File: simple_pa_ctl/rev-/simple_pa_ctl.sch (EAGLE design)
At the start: 93 parts, among them IC1 LD117ADT50TR, IC2 MCP9700, IC3 ATMEGA32U4-AU, J1 USB_B_PTH, K3 G5V1, SW1 SPST_TACT-KMR2, Y1 8MHz

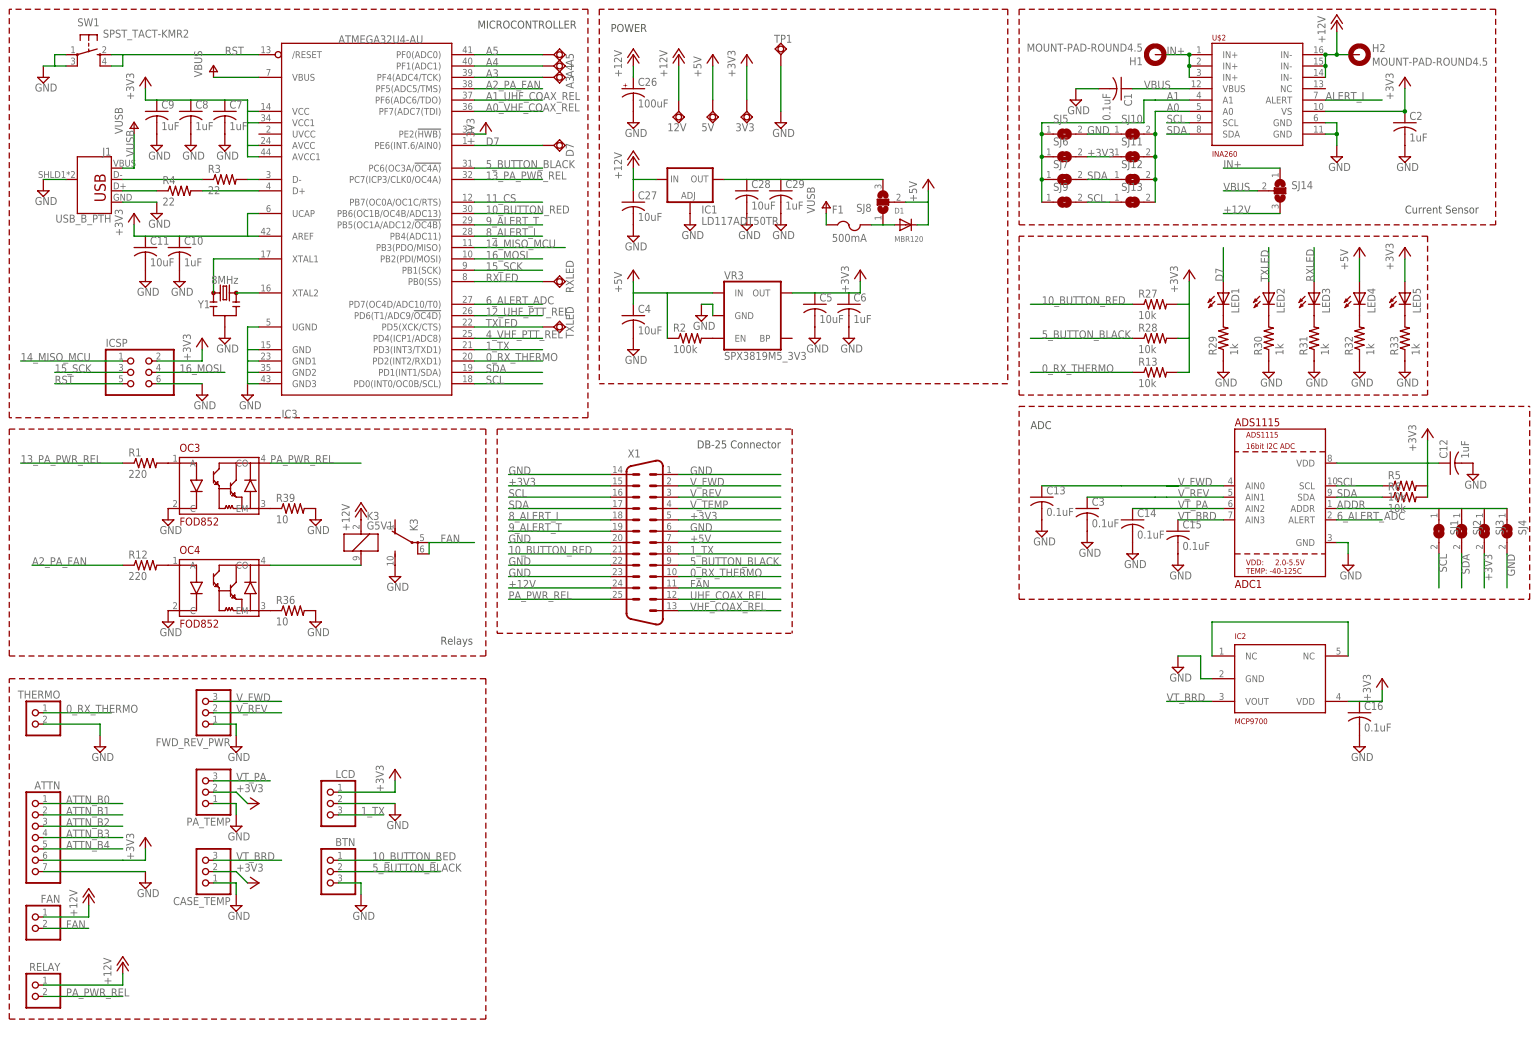
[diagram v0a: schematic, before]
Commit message: very simple, featherwing footprint
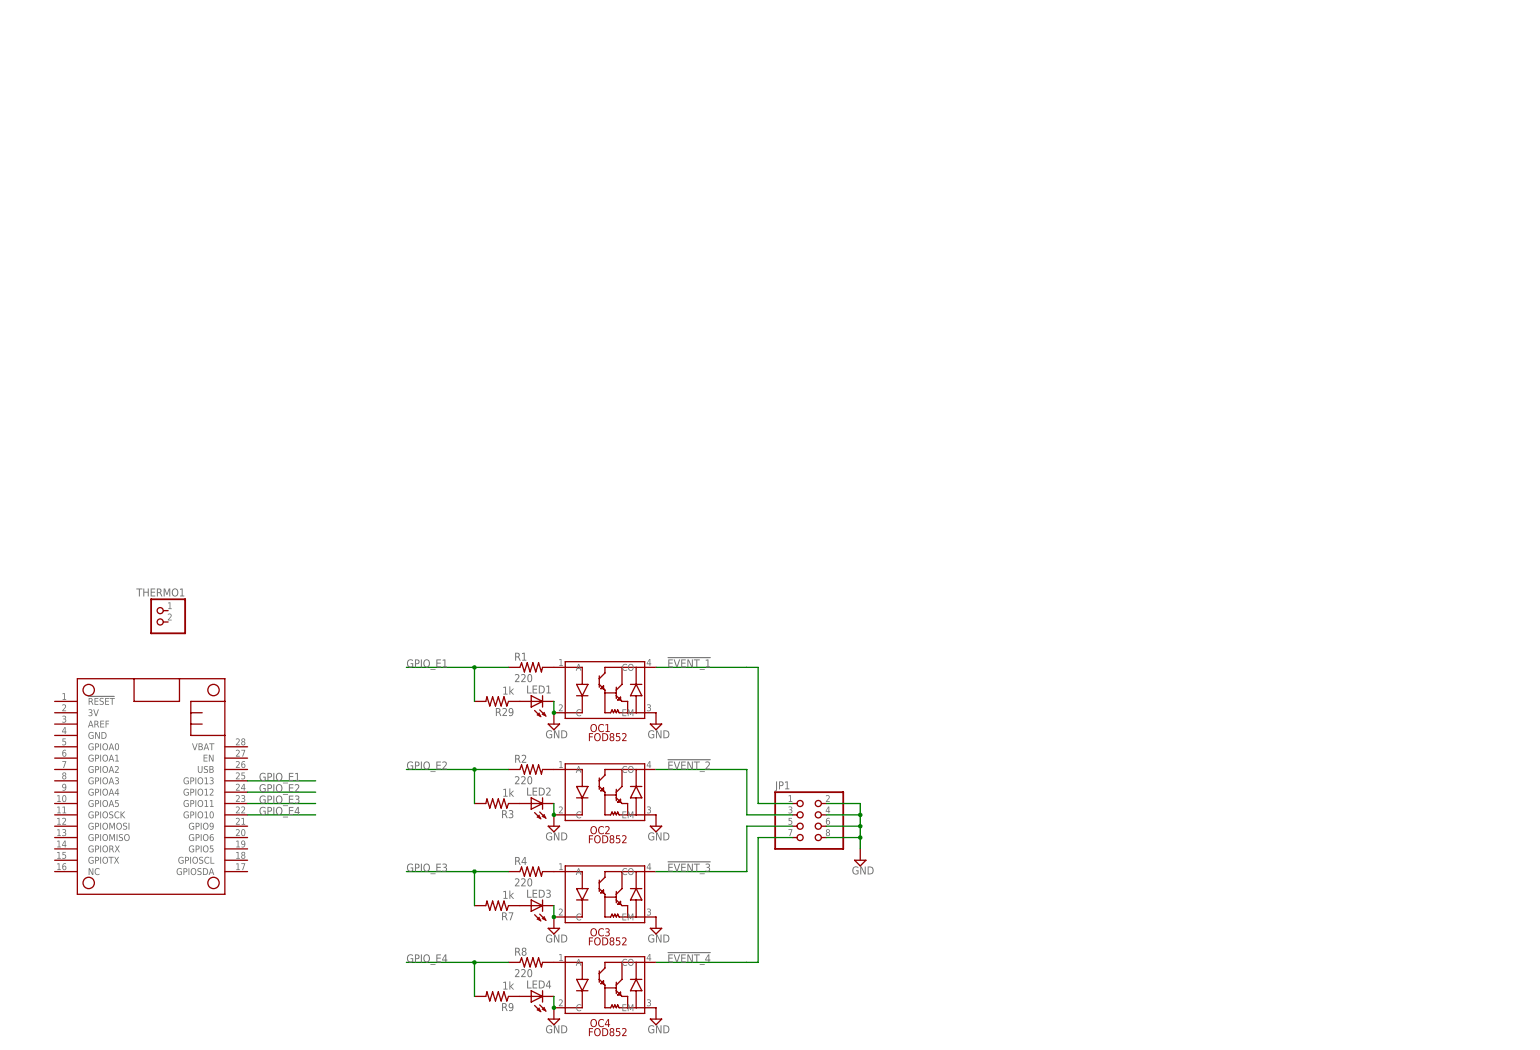
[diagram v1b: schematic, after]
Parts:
- removed 12V, 3V3, 5V, A3, A4, A5, D7, RXLED, TP1, TXLED: TPSQTP20SQ, testpad:TPSQTP20SQ
- removed ADC1: ADS1115, vtgs:ADS1115
- removed ATTN: (no value), pinhead:PINHD-1X7
- removed BTN, CASE_TEMP, FWD_REV_PWR, LCD, PA_TEMP: (no value), pinhead:PINHD-1X3
- removed C1, C13, C14, C15, C16, C3: 0.1uF, rcl:C-USC0805K
- removed C10, C12, C2, C29, C6, C7, C8, C9: 1uF, rcl:C-USC0805K
- removed C11, C27, C28, C4, C5: 10uF, rcl:C-USC0805K
- removed C26: 100uF, rcl:CPOL-USD
- removed D1: MBR120, adafruit:DIODESOD-123
- removed F1: 500mA, adafruit:PTCFUSE-1206
- removed FAN, RELAY, THERMO: (no value), pinhead:PINHD-1X2
- removed H1, H2: MOUNT-PAD-ROUND4.5, holes:MOUNT-PAD-ROUND4.5
- removed IC1: LD117ADT50TR, v-reg:LD117ADT50TR
- removed IC2: MCP9700, vtgs:MCP9700
- removed IC3: ATMEGA32U4-AU, adafruit:ATMEGA32U4-AU
- removed ICSP: (no value), pinhead:PINHD-2X3
- removed J1: USB_B_PTH, SparkFun-Connectors:USB_B_PTH
- removed K3: G5V1, relay:G5V1
- removed LED5: (no value), adafruit:LEDCHIPLED_0805
- removed R12: 220, rcl:R-US_R0805
- removed R13, R27, R28, R5, R6: 10k, rcl:R-US_R0805
- removed R30, R31, R32, R33: 1k, rcl:R-US_R0805
- removed R36, R39: 10, rcl:R-US_R0805
- removed SJ1, SJ10, SJ11, SJ12, SJ13, SJ2, SJ3, SJ4, SJ5, SJ6, SJ7, SJ9: (no value), jumper:SJ
- removed SJ14, SJ8: (no value), jumper:SJ2W
- removed SW1: SPST_TACT-KMR2, adafruit:SPST_TACT-KMR2
- removed U$2: INA260, vtgs:INA260
- removed VR3: SPX3819M5_3V3, kj4qlp:V_REG_SPX3819-SOT23-5
- removed X1: (no value), SparkFun-Retired:DB25_MALEVB
- removed Y1: 8MHz, SparkFun-Clocks:RESONATOR-8MHZSMD_3.2X1.3
- added JP1: (no value), pinhead:PINHD-2X4
- added MS1: FEATHERWING, adafruit:FEATHERWING
- added OC1, OC2: FOD852, vtgs:FOD852
- added R7, R9: 1k, rcl:R-US_R0805
- added R8: 220, rcl:R-US_R0805
- added THERMO1: (no value), pinhead:PINHD-1X2
- R2: value 100k -> 220
- R3: value 22 -> 1k
- R4: value 22 -> 220
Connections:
- removed net +12V: 12V.TP, C26.+, C27.1, FAN.1, H2.MOUNT, IC1.IN, K31.1, RELAY.1, SJ14.3, U$2.IN-@1, U$2.IN-@2, U$2.IN-@3, X1.24
- removed net +3V3: 3V3.TP, ADC1.VDD, ATTN.6, C10.1, C11.1, C12.1, C16.1, C2.1, C5.1, C6.1, C7.1, C8.1, C9.1, CASE_TEMP.2, IC2.VDD, IC3.AREF, IC3.AVCC, IC3.AVCC1, IC3.PE2(!HWB), IC3.UCAP, IC3.VCC, IC3.VCC1, ICSP.2, LCD.1, LED5.A, PA_TEMP.2, R13.2, R27.2, R28.2, R5.2, R6.2, SJ11.1, SJ3.2, SJ6.2, U$2.VS, VR3.OUT, X1.15, X1.5
- removed net +5V: 5V.TP, C4.1, D1.C, LED4.A, R2.1, SJ8.2, VR3.IN, X1.7
- removed net 0_RX_THERMO: IC3.PD2(INT2/RXD1), R13.1, THERMO.1, X1.10
- removed net 10_BUTTON_RED: BTN.1, IC3.PB6(OC1B/OC4B/ADC13), R27.1, X1.21
- removed net 11_CS: IC3.PB7(OC0A/OC1C/RTS)
- removed net 12_UHF_PTT_REL: IC3.PD6(T1/ADC9/!OC4D)
- removed net 13_PA_PWR_REL: IC3.PC7(ICP3/CLK0/OC4A), R1.1
- removed net 14_MISO_MCU: IC3.PB3(PDO/MISO), ICSP.1
- removed net 15_SCK: IC3.PB1(SCK), ICSP.3
- removed net 16_MOSI: IC3.PB2(PDI/MOSI), ICSP.4
- removed net 1_TX: IC3.PD3(INT3/TXD1), LCD.3, X1.8
- removed net 4_VHF_PTT_REL: IC3.PD4(ICP1/ADC8)
- removed net 5_BUTTON_BLACK: BTN.2, IC3.PC6(OC3A/!OC4A), R28.1, X1.9
- removed net 6_ALERT_ADC: ADC1.ALERT, IC3.PD7(OC4D/ADC10/T0)
- removed net 8_ALERT_I: IC3.PB4(ADC11), X1.18
- removed net 9_ALERT_T: IC3.PB5(OC1A/ADC12/!OC4B), X1.19
- removed net A0: SJ10.2, SJ11.2, SJ12.2, SJ13.2, U$2.A0
- removed net A0_VHF_COAX_REL: IC3.PF7(ADC7(TDI)
- removed net A1: SJ5.1, SJ6.1, SJ7.1, SJ9.1, U$2.A1
- removed net A1_UHF_COAX_REL: IC3.PF6(ADC6/TDO)
- removed net A2_PA_FAN: IC3.PF5(ADC5/TMS), R12.1
- removed net A3: A3.TP, IC3.PF4(ADC4/TCK)
- removed net A4: A4.TP, IC3.PF1(ADC1)
- removed net A5: A5.TP, IC3.PF0(ADC0)
- removed net ADDR: ADC1.ADDR, SJ1.1, SJ2.1, SJ3.1, SJ4.1
- removed net ALERT_I: U$2.ALERT
- removed net ATTN_B0: ATTN.1
- removed net ATTN_B1: ATTN.2
- removed net ATTN_B2: ATTN.3
- removed net ATTN_B3: ATTN.4
- removed net ATTN_B4: ATTN.5
- removed net D7: D7.TP, IC3.PE6(INT.6/AIN0), LED1.A
- removed net FAN: FAN.2, K32.P, K32.P@1, X1.11
- removed net IN+: H1.MOUNT, SJ14.1, U$2.IN+@1, U$2.IN+@2, U$2.IN+@3
- removed net N$10: IC3.D+, R4.2
- removed net N$11: J1.D+, R4.1
- removed net N$16: LED1.C, R29.2
- removed net N$17: LED2.C, R30.2
- removed net N$18: LED4.C, R32.2
- removed net N$19: LED5.C, R33.2
- removed net N$21: OC4.A, R12.2
- removed net N$24: LED3.C, R31.2
- removed net N$27: OC4.EM, R36.1
- removed net N$31: C28.1, C29.1, IC1.OUT, SJ8.3
- removed net N$39: D1.A, F1.2, SJ8.1
- removed net N$40: OC3.EM, R39.1
- removed net N$9: IC3.D-, R3.2
- removed net PA_PWR_REL: OC3.CO, RELAY.2, X1.25
- removed net RST: IC3./RESET, ICSP.5, SW1.S, SW1.S1
- removed net RXLED: IC3.PB0(SS), LED3.A, RXLED.TP
- removed net SCL: ADC1.SCL, IC3.PD0(INT0/OC0B/SCL), R5.1, SJ1.2, SJ13.1, SJ9.2, U$2.SCL, X1.16
- removed net SDA: ADC1.SDA, IC3.PD1(INT1/SDA), R6.1, SJ12.1, SJ2.2, SJ7.2, U$2.SDA, X1.17
- removed net TXLED: IC3.PD5(XCK/CTS), LED2.A, TXLED.TP
- removed net UHF_COAX_REL: X1.12
- removed net VBUS: C1.1, SJ14.2, U$2.VBUS
- removed net VHF_COAX_REL: X1.13
- removed net VT_BRD: ADC1.AIN3, C15.1, CASE_TEMP.3, IC2.VOUT
- removed net VT_PA: ADC1.AIN2, C14.1, PA_TEMP.3
- removed net VUSB: F1.1, IC3.VBUS, J1.VBUS
- removed net V_FWD: ADC1.AIN0, C13.1, FWD_REV_PWR.3, X1.2
- removed net V_REV: ADC1.AIN1, C3.1, FWD_REV_PWR.2, X1.3
- removed net V_TEMP: X1.4
- new net !EVENT_1: JP1.1, OC1.CO
- new net !EVENT_2: JP1.3, OC2.CO
- new net !EVENT_3: JP1.5, OC3.CO
- new net !EVENT_4: JP1.7, OC4.CO
- new net GPIO_E1: MS1.GPIO13, R1.1, R29.2
- new net GPIO_E2: MS1.GPIO12, R2.1, R3.2
- new net GPIO_E3: MS1.GPIO11, R4.1, R7.2
- new net GPIO_E4: MS1.GPIO10, R8.1, R9.2
- new net N$7: OC4.A, R8.2
- net GND: now also JP1.2, JP1.4, JP1.6, JP1.8, LED1.C, LED2.C, LED3.C, LED4.C, OC1.C, OC1.EM, OC2.C, OC2.EM, OC3.EM, OC4.EM; no longer ADC1.GND, ATTN.7, BTN.3, C1.2, C10.2, C11.2, C12.2, C13.2, C14.2, C15.2, C16.2, C2.2, C26.-, C27.2, C28.2, C29.2, C3.2, C4.2, C5.2, C6.2, C7.2, C8.2, C9.2, CASE_TEMP.1, FWD_REV_PWR.1, IC1.ADJ, IC2.GND, IC3.GND, IC3.GND1, IC3.GND2, IC3.GND3, IC3.UGND, ICSP.6, J1.GND, J1.SHIELD, K32.S, LCD.2, PA_TEMP.1, R29.1, R30.1, R31.1, R32.1, R33.1, R36.2, R39.2, SJ10.1, SJ4.2, SJ5.2, SW1.P, SW1.P1, THERMO.2, TP1.TP, U$2.GND@1, U$2.GND@2, VR3.GND, X1.1, X1.14, X1.20, X1.22, X1.23, X1.6, Y1.2
- net N$1: now also OC1.A; no longer OC3.A
- net N$2: now also LED1.A, R29.1; no longer K31.2, OC4.CO
- net N$3: now also OC2.A; no longer VR3.EN
- net N$4: now also LED2.A, R3.1; no longer IC3.XTAL1, Y1.1
- net N$5: now also OC3.A, R4.2; no longer IC3.XTAL2, Y1.3
- net N$6: now also LED3.A, R7.1; no longer IC2.NC@1, IC2.NC@5
- net N$8: now also LED4.A, R9.1; no longer J1.D-, R3.1
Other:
- note removed: "ADC"
- note removed: "Current Sensor"
- note removed: "DB-25 Connector"
- note removed: "MICROCONTROLLER"
- note removed: "POWER"
- note removed: "Relays"
- moved on the sheet: LED1, LED2, LED3, LED4, OC3, OC4, R1, R2, R29, R3, R4
